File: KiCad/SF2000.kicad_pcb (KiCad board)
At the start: 4 copper layers, 111.5 x 83.9 mm, 108 parts, among them J1 Conn_2Rows-86Pins_even_odd, J10 Conn_02x01, J11 Conn_02x01, J2 Conn_01x02, J20 Conn_02x11_Odd_Even, J3 Conn_02x05_Odd_Even, J4 Conn_02x01, J5 Conn_01x01, J6 Micro_SD_Card_Socket, J7 Conn_02x01, J8 Conn_02x01, J9 Conn_02x01, Q1 MMBT3904, Q2 MMBT3906, U1 LM1117-3.3, U10 IS61WV20488FBLL-10TLI, U11 IS61WV20488FBLL-10TLI, U12 IS61WV20488FBLL-10TLI, U13 IS61WV20488FBLL-10TLI, U14 SST39LF040, U15 SST39LF802C, U16 74AHCT3G14, U2 ABLIC S-1132B43-M5T1U, U20 AT25SF081B-SSH, U3 TLV74312PDBV, U4 SN74CBT16211, U5 SN74CBT16211, U6 SN74CBT16211, U7 SN74AUP1T87DCKR, U8 T8Q144C3, U9 68000D, X1 Oscillator_7.0x5.0mm

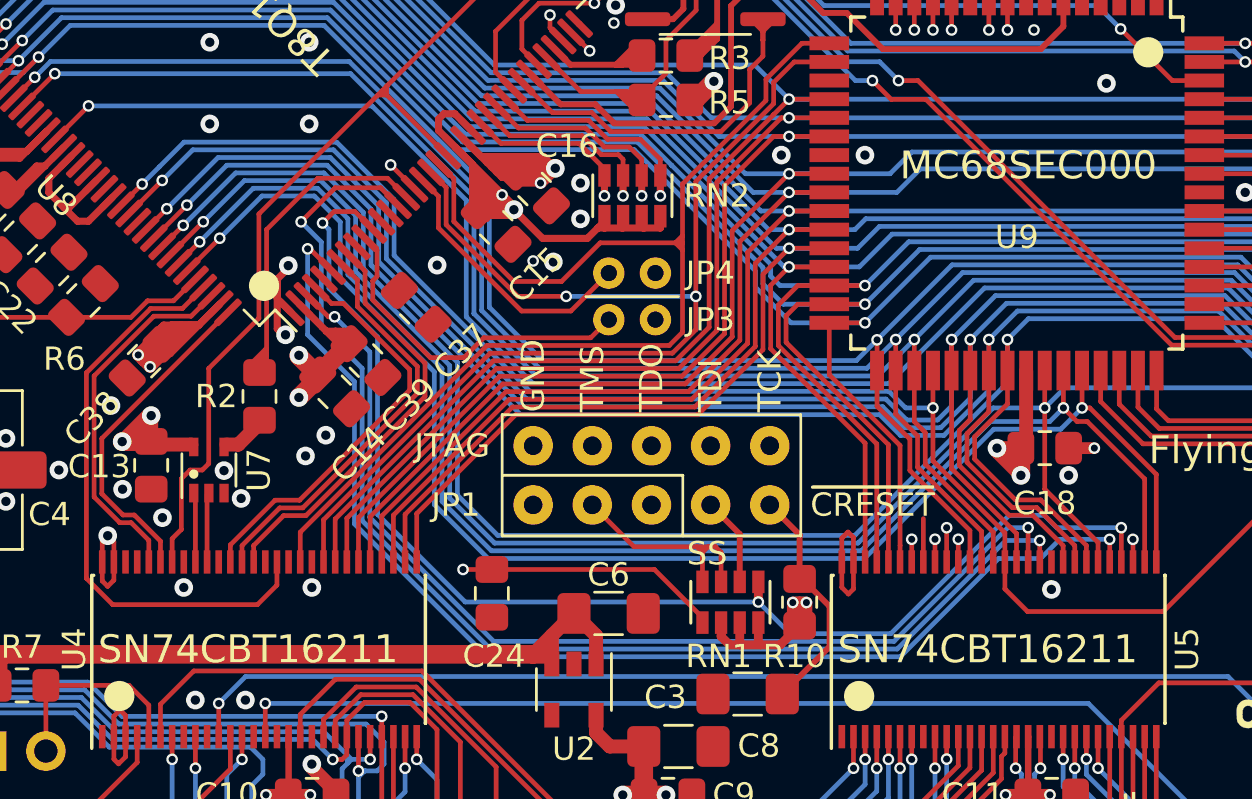
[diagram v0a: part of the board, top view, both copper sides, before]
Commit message: Route C37 decoupling power supply to pin 12 FPGA
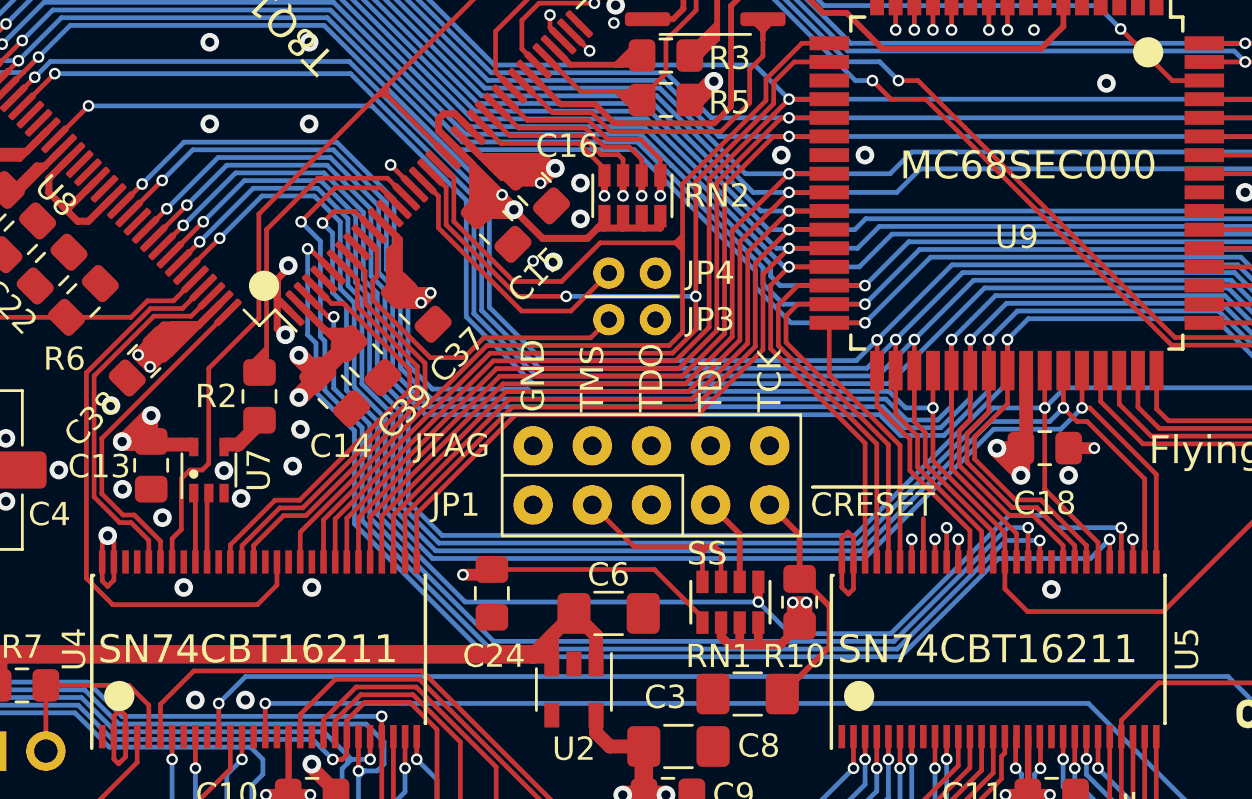
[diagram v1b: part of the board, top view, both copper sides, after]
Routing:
- net 3V3: track 293.7 -> 306.3 mm, vias 53 -> 54
- net A17_3V3: track 167.9 -> 170.3 mm
- net A16_3V3: track 178.1 -> 180.5 mm
- net A18_3V3: track 168.9 -> 171.3 mm
- net A19_3V3: track 134.9 -> 137.3 mm
- net A22_3V3: track 63.0 -> 64.4 mm
- net A21_3V3: track 133.8 -> 135.2 mm
- net A20_3V3: track 141.2 -> 142.6 mm
- net A23_3V3: track 63.4 -> 64.8 mm

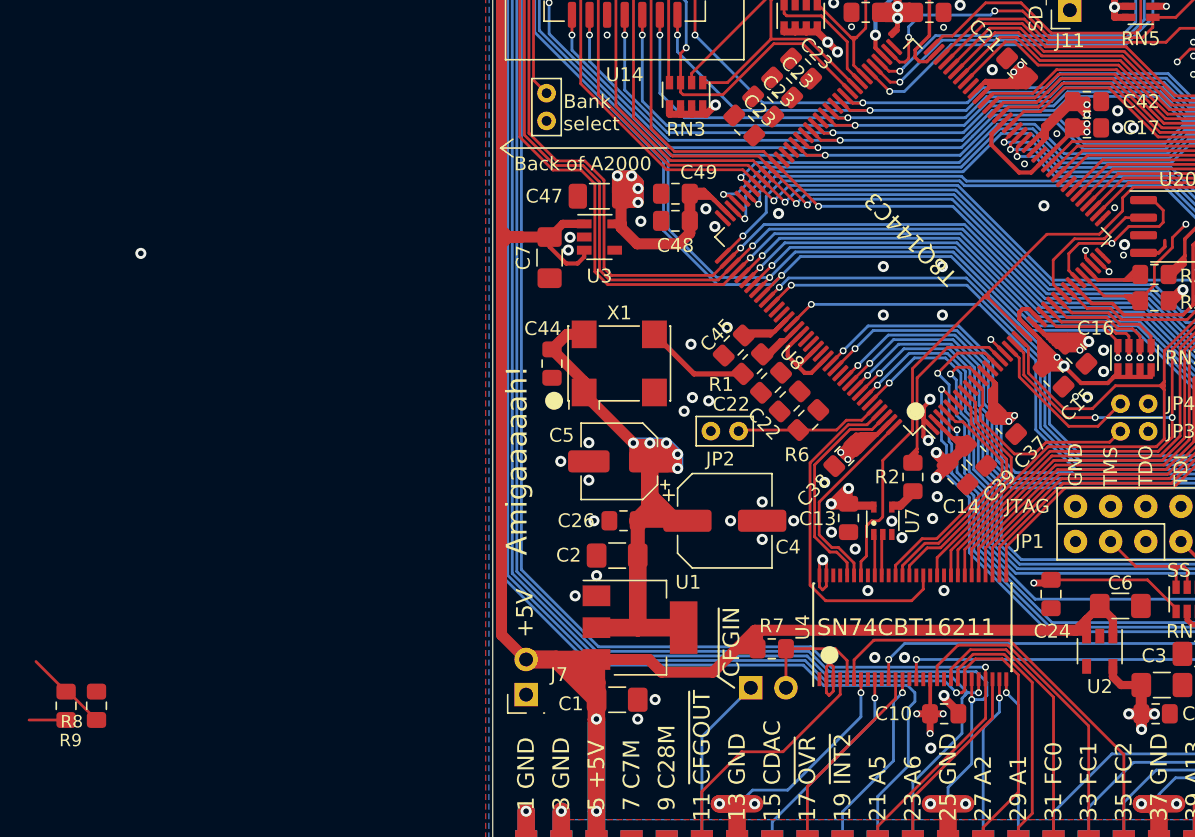
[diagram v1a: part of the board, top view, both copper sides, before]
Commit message: Placement of C23 decoupling cap and routing of 1.2V supply to pin 13
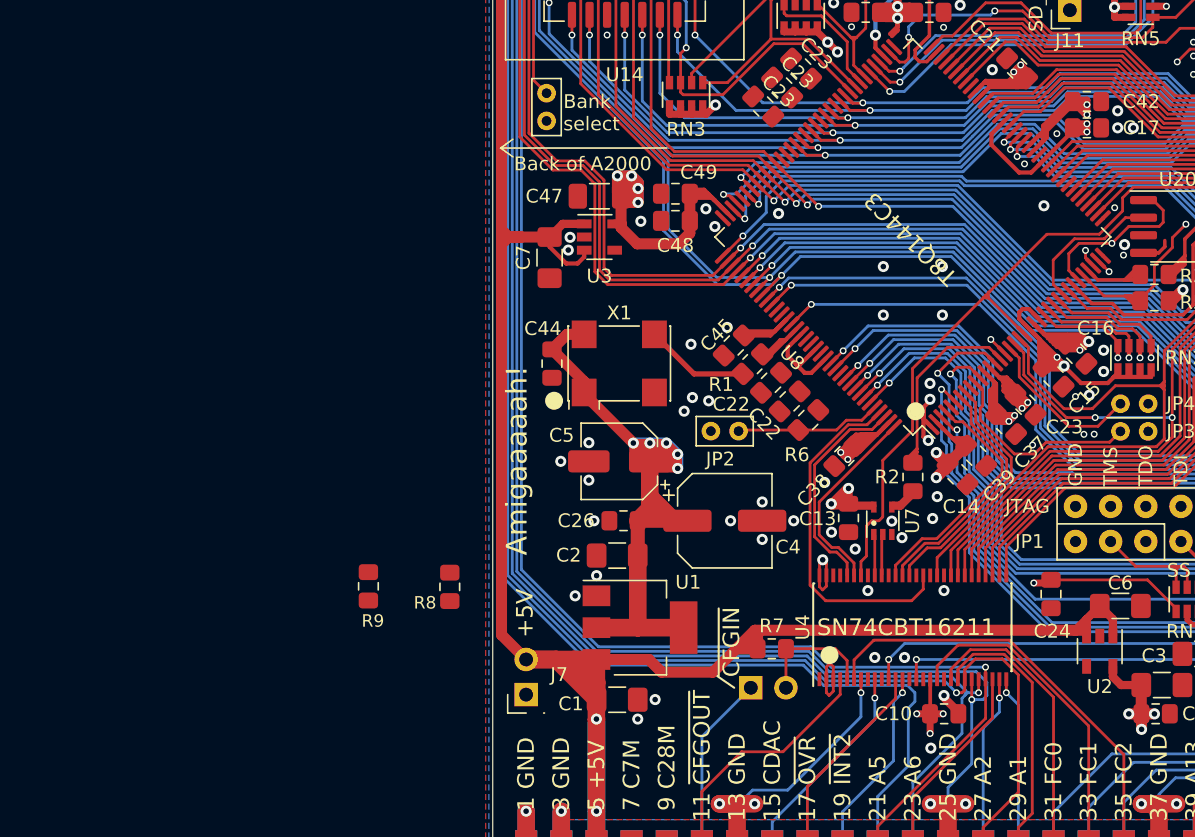
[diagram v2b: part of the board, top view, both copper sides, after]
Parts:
- moved C23 28.6 mm to (136.1, 104.7), turned to 135 degrees
- moved R8 26.9 mm to (94.6, 117.9)
- moved R9 23.5 mm to (88.7, 117.8)
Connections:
- C23 pad 2: 3V3 -> 1V2 (x4)
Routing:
- net 1V2: track 85.2 -> 98.3 mm, vias 10 -> 12
- net Net-(R8-Pad2): track 5.97 -> 0.00 mm
- net Net-(R9-Pad1): track 2.67 -> 0.00 mm
- net GND: vias 119 -> 123
- net 3V3: vias 54 -> 53

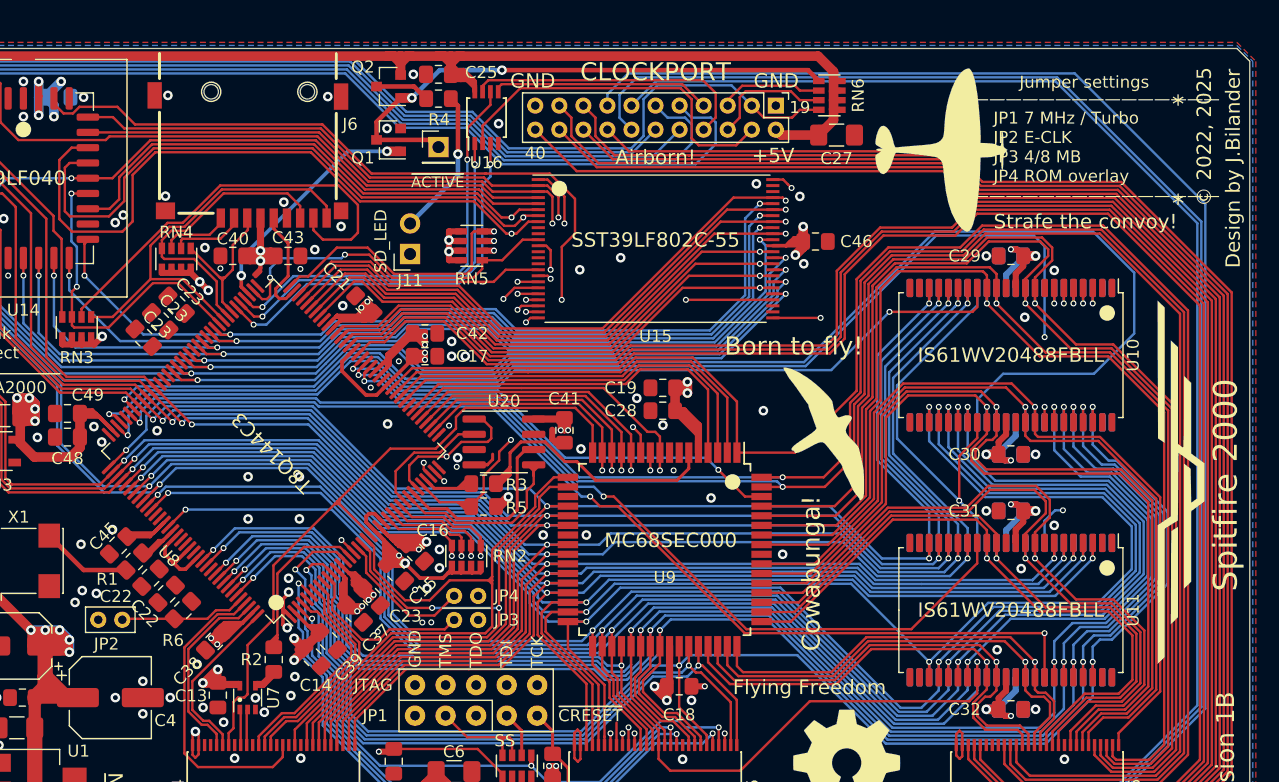
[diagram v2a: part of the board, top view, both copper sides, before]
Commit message: Routing 3.3V power via C45 bypass cap to FPGA pin 122
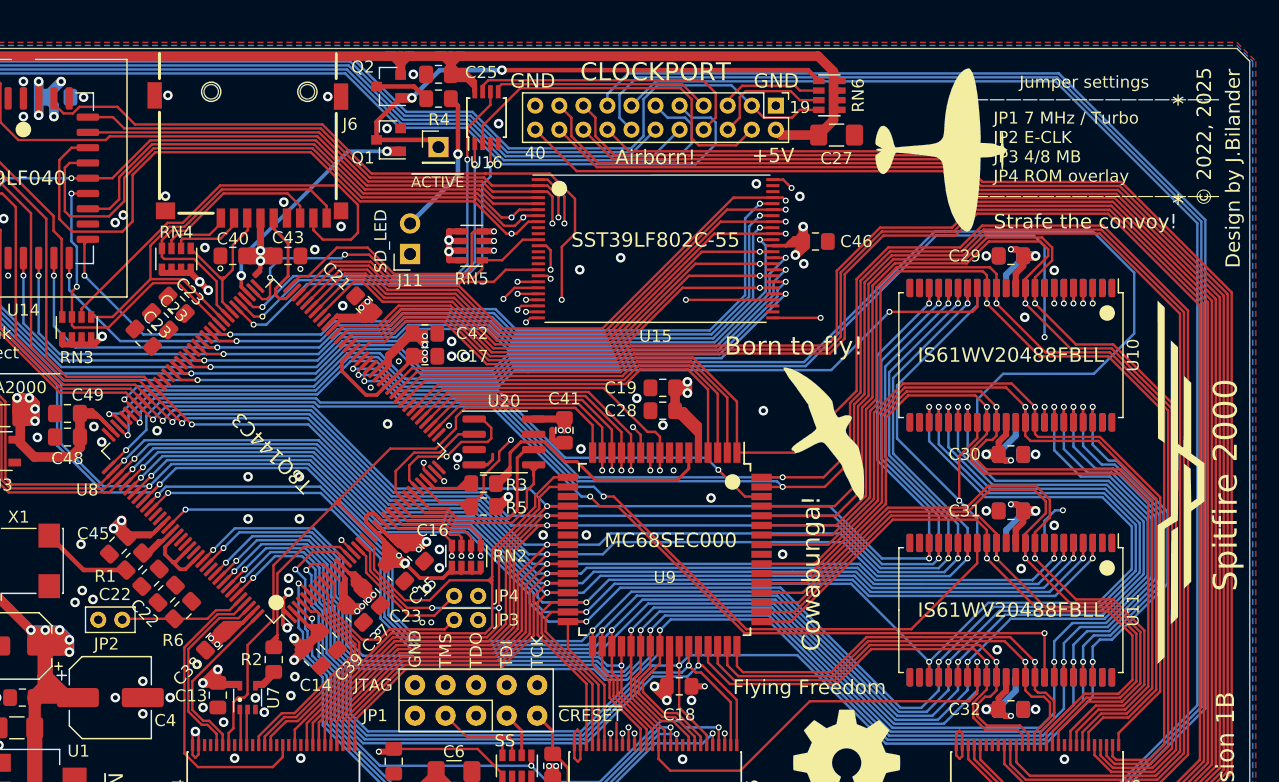
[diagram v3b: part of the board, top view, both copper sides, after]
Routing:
- net 3V3: track 306.3 -> 310.2 mm, vias 53 -> 54
- net D5: track 134.8 -> 134.0 mm

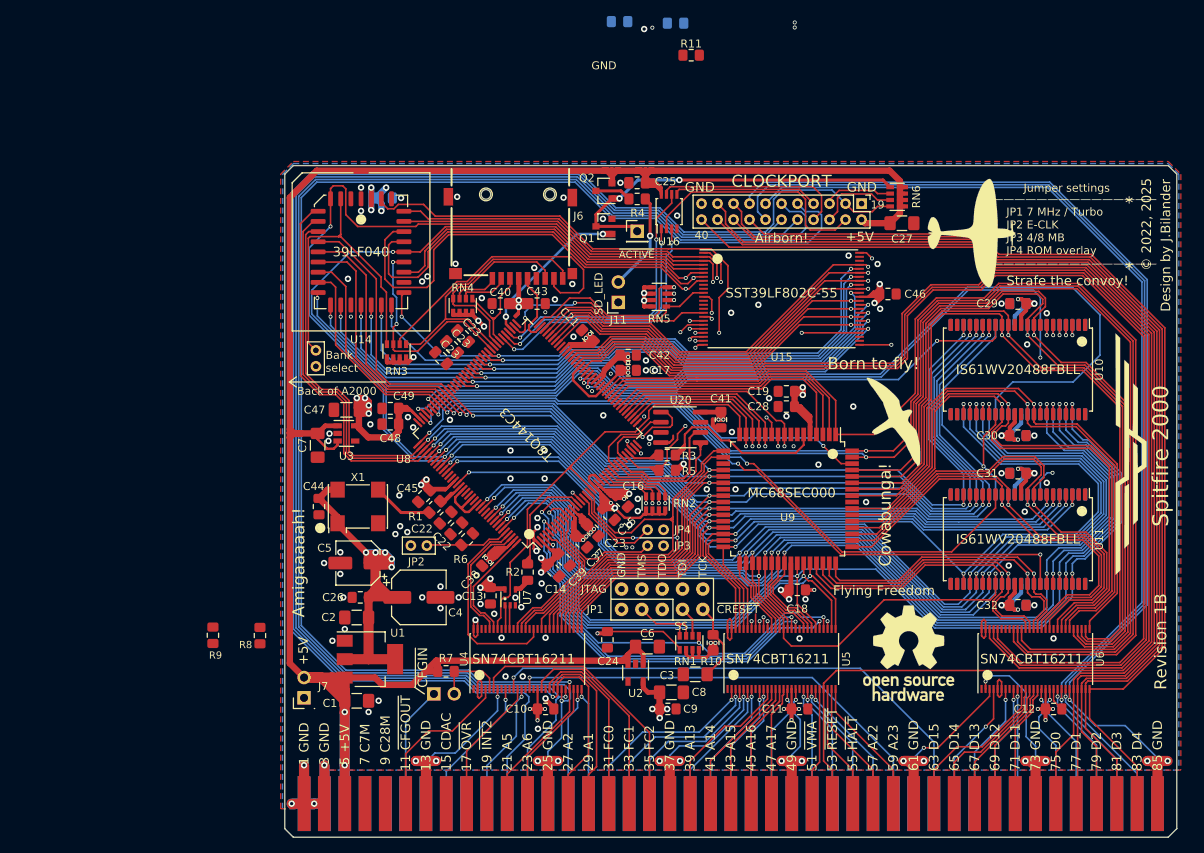
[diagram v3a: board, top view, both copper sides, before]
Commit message: Remove R12,R13
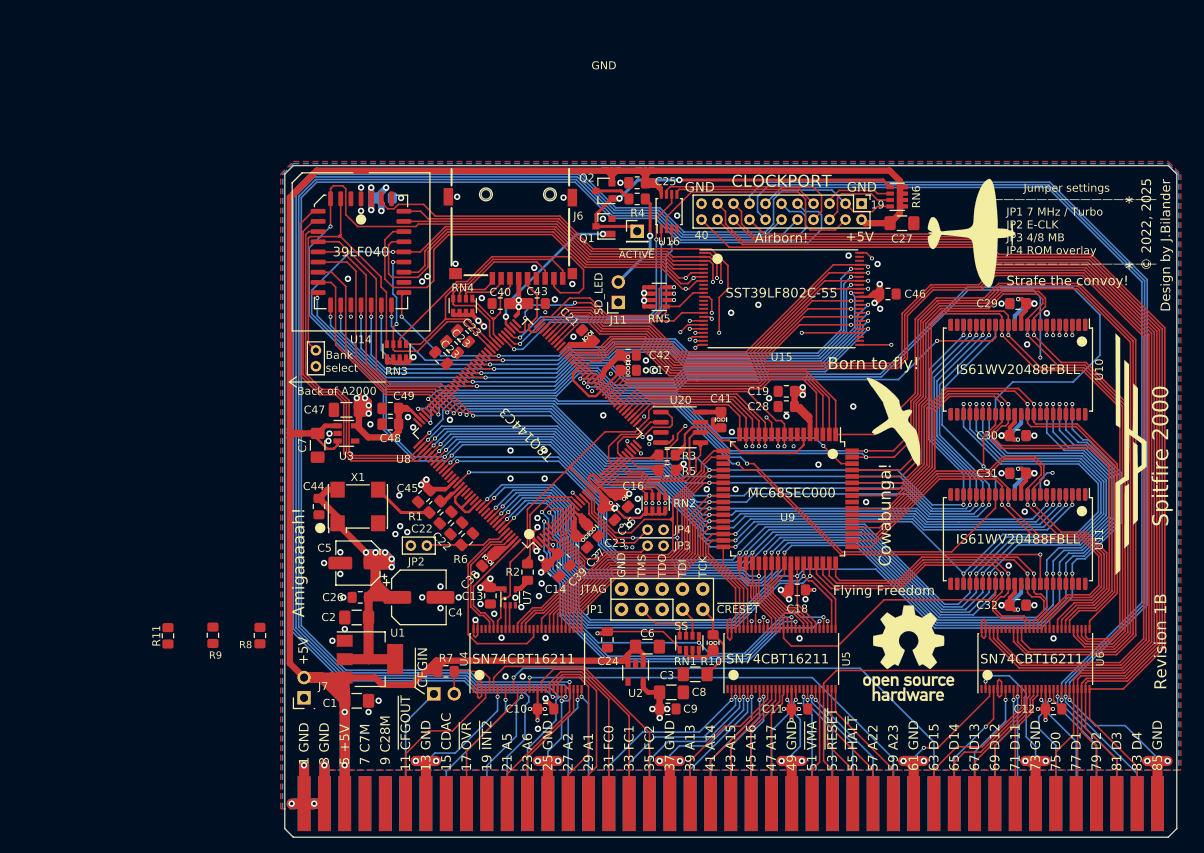
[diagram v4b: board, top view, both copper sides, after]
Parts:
- removed R12: 1k, Resistor_SMD:R_0805_2012Metric_Pad1.15x1.40mm_HandSolder
- removed R13: 4.7k, Resistor_SMD:R_0805_2012Metric_Pad1.15x1.40mm_HandSolder
- moved R11 97.7 mm to (83.1, 117.9), turned to 270 degrees
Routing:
- net +5VDC: track 269.8 -> 271.6 mm
- net 3V3: vias 54 -> 50

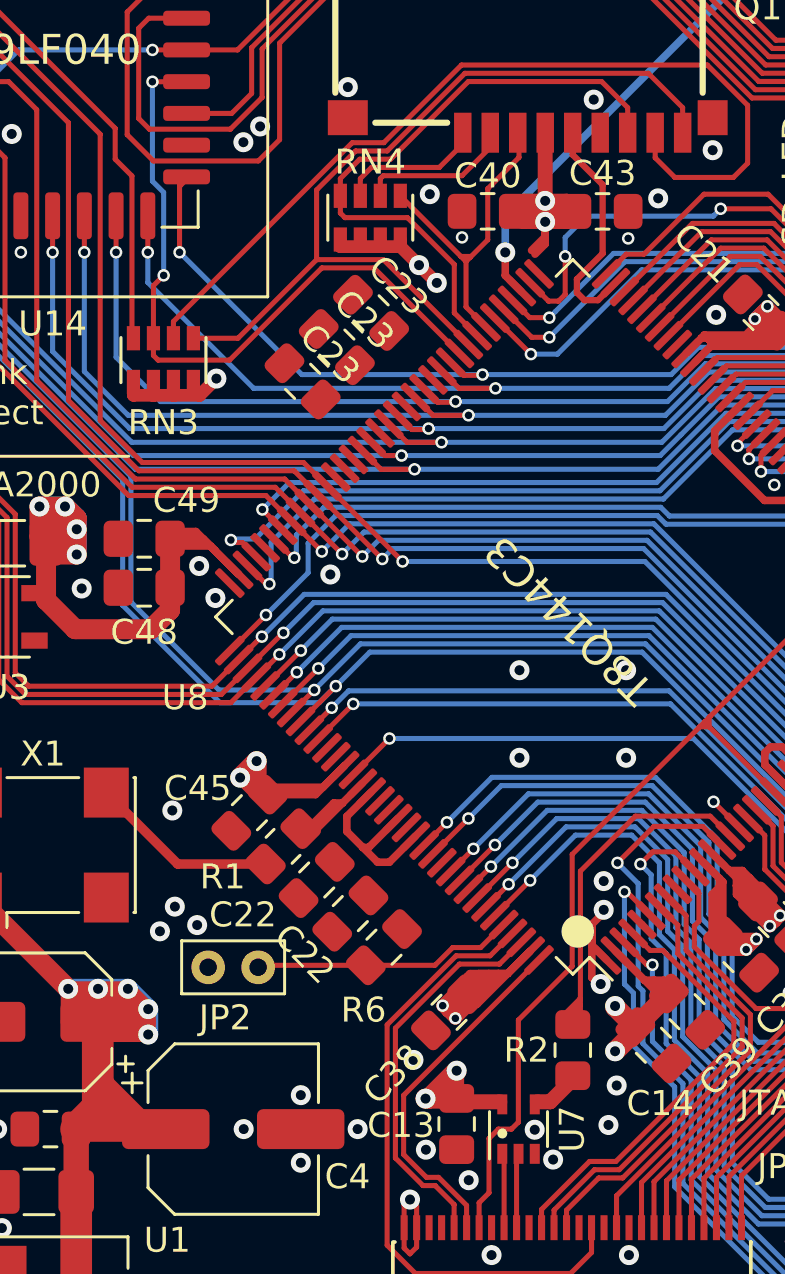
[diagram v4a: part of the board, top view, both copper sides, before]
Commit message: Routing of 1.2V supply to FPGA pins 125,128,130 via decoupling caps C22, C40
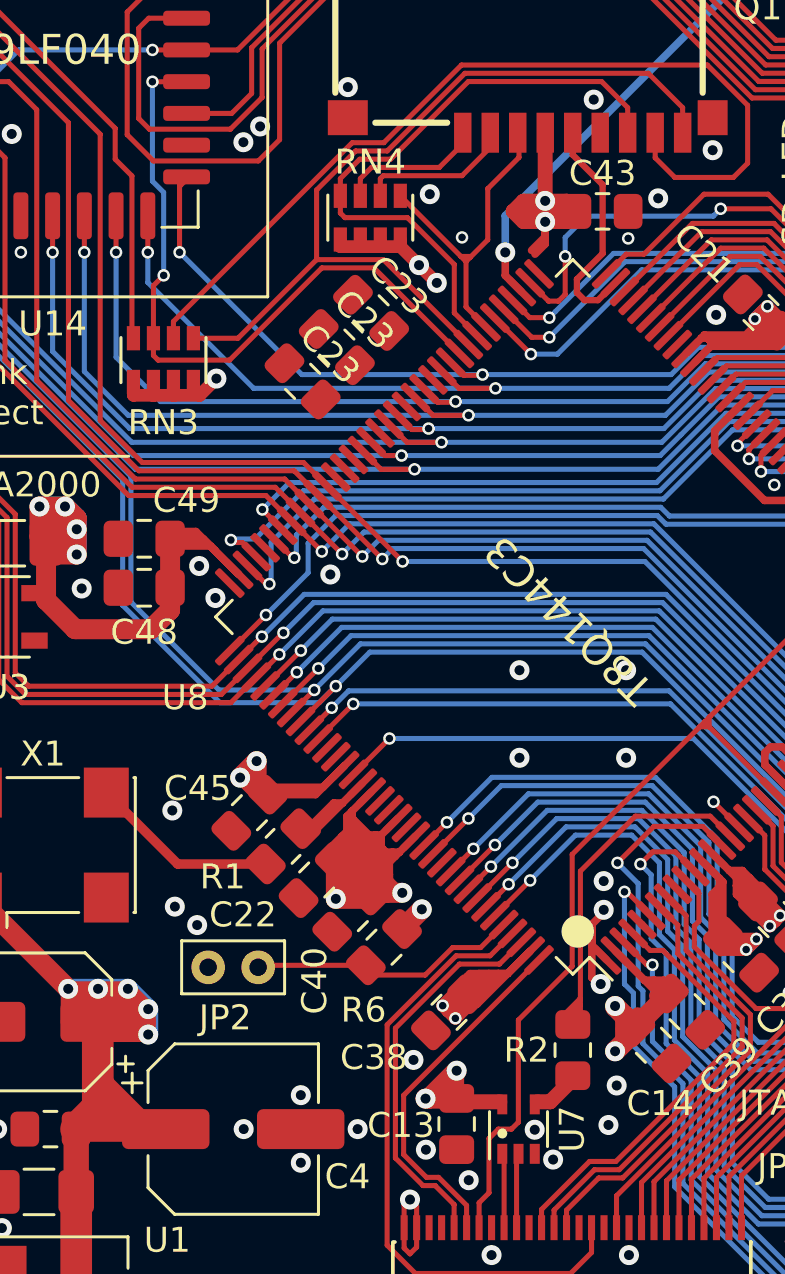
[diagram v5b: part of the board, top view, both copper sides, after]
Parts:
- removed the C22 at (119.1, 104.5)
- moved C40 28.6 mm to (119.1, 104.5), turned to 45 degrees
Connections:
- C22 pad 2: 3V3 -> 1V2
- C40 pad 2: 3V3 -> 1V2
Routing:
- net 1V2: track 98.3 -> 132.9 mm, vias 12 -> 14
- net 3V3: track 310.2 -> 311.3 mm
